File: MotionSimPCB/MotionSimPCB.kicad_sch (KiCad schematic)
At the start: 26 parts, among them J1 Conn_01x02, J10 Conn_01x02, J12 AudioJack2, J2 Conn_01x08_Pin, J3 Conn_01x03, J4 Conn_01x03, J5 Conn_01x03, J6 Conn_01x03, J7 Conn_01x02, J8 Conn_01x02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

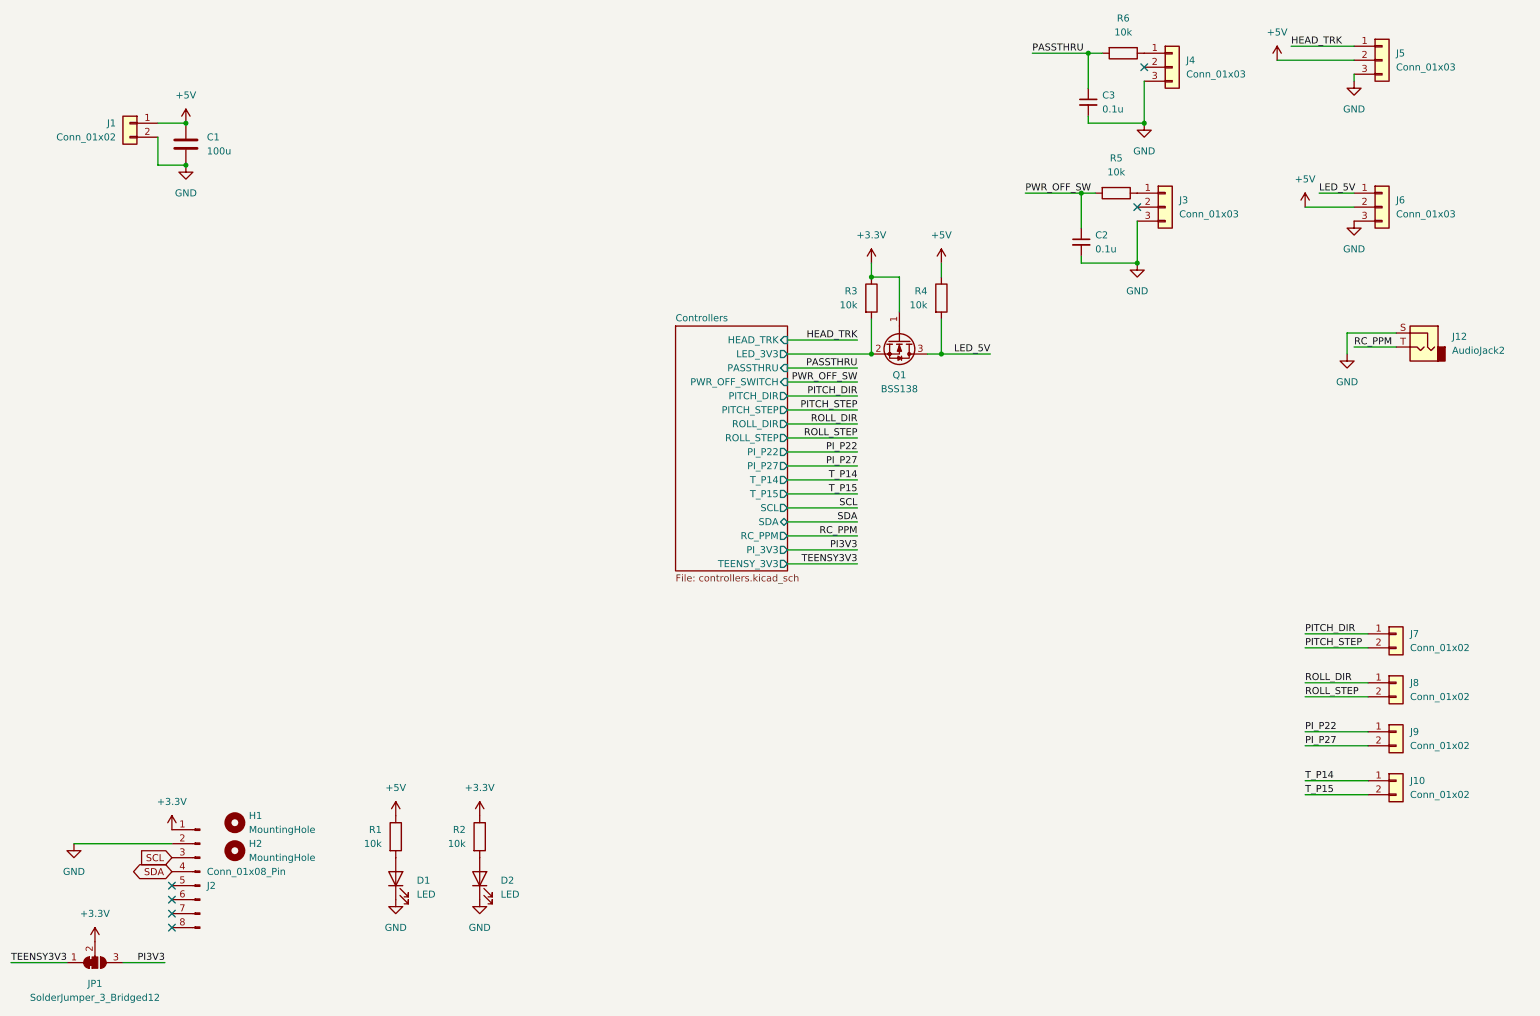
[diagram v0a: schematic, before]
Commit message: fix drc, add protection
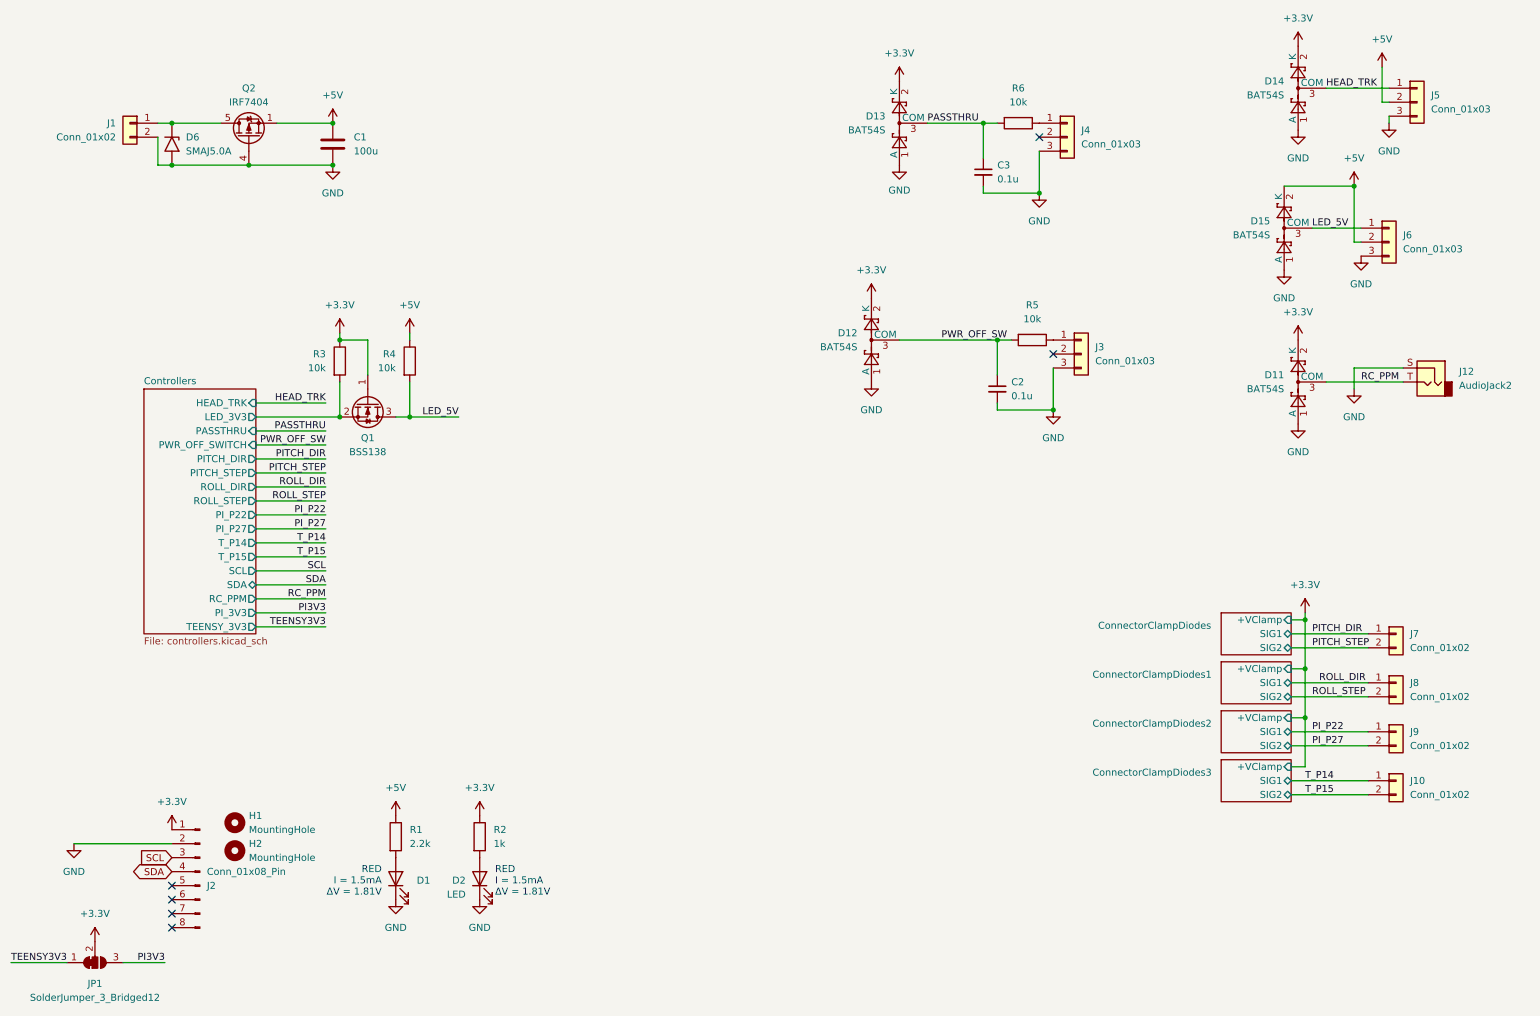
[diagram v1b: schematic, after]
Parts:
- added D11, D12, D13, D14, D15: BAT54S, Package_TO_SOT_SMD:SOT-23, symbol Diode:BAT54S
- added D6: SMAJ5.0A, Diode_SMD:D_SMA, symbol Diode:SMAJ5.0A
- added Q2: IRF7404, Package_SO:SOIC-8_3.9x4.9mm_P1.27mm, symbol Transistor_FET:IRF7404
- D1, D2: JLC PN (none) -> C2286
- R1: value 10k -> 2.2k
- R2: value 10k -> 1k
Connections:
- net +3.3V: now also D11.2 (K), D12.2 (K), D13.2 (K), D14.2 (K)
- net +5V: now also D15.2 (K), Q2.1 (S), Q2.2 (S), Q2.3 (S); no longer J1.1 (Pin_1)
- net GND: now also D11.1 (A), D12.1 (A), D13.1 (A), D14.1 (A), D15.1 (A), D6.2 (A2), Q2.4 (G)
- net HEAD_TRK: now also D14.3 (COM)
- net LED_5V: now also D15.3 (COM)
- net PASSTHRU: now also D13.3 (COM)
- net PWR_OFF_SW: now also D12.3 (COM)
- net RC_PPM: now also D11.3 (COM)
- new net: D6.1 (A1), J1.1 (Pin_1), Q2.5 (D), Q2.6 (D), Q2.7 (D), Q2.8 (D)
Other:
- added sheet ConnectorClampDiodes (connector_clamp_diodes.kicad_sch)
- added sheet ConnectorClampDiodes1 (connector_clamp_diodes.kicad_sch)
- added sheet ConnectorClampDiodes2 (connector_clamp_diodes.kicad_sch)
- added sheet ConnectorClampDiodes3 (connector_clamp_diodes.kicad_sch)
- note added: "RED I = 1.5mA ΔV = 1.81V"
- moved on the sheet: C1, C2, C3, J12, J3, J4, J5, J6, Q1, R3, R4, R5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

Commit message: fix some issues
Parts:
- added C8: 0.1u, Capacitor_SMD:C_0603_1608Metric, symbol Device:C
- added D16: BZV55C12, Diode_SMD:D_MiniMELF, symbol Diode:BZV55C12
- added JP2: SolderJumper_2_Open, Jumper:SolderJumper-2_P1.3mm_Open_TrianglePad1.0x1.5mm, symbol Jumper:SolderJumper_2_Open
- added R13: 100, Capacitor_SMD:C_0603_1608Metric, symbol Device:R
- added R14: 100k, Capacitor_SMD:C_0603_1608Metric, symbol Device:R
- added TP1: TestPoint_Flag, TestPoint:TestPoint_Pad_D2.0mm, symbol Connector:TestPoint_Flag
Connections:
- net +3.3V: now also R5.1, R6.1
- net +5V: now also C8.1, D16.1 (K), JP2.2 (B), R14.1, TP1.1
- net GND: now also R13.2; no longer Q2.4 (G)
- net PASSTHRU: now also J4.1 (Pin_1)
- net PWR_OFF_SW: now also J3.1 (Pin_1)
- net at D6.1 (A1), J1.1 (Pin_1), Q2.5 (D)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: now also JP2.1 (A)
- new net: C8.2, D16.2 (A), Q2.4 (G), R13.1, R14.2
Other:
- moved on the sheet: C1, Q1, Q2, R3, R4, R5, R6

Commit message: fix clearance
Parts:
- added R15, R16, R17, R18, R19, R20, R21, R22, R24, R25: 100, Capacitor_SMD:C_0603_1608Metric, symbol Device:R
- Q2: value IRF7404 -> DMP2040USS
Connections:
- net HEAD_TRK: now also R25.1; no longer D14.3 (COM), J5.1 (Pin_1)
- net PITCH_DIR: now also R15.1; no longer J7.1 (Pin_1)
- net PITCH_STEP: now also R16.1; no longer J7.2 (Pin_2)
- net PI_P22: now also R19.1; no longer J9.1 (Pin_1)
- net PI_P27: now also R20.1; no longer J9.2 (Pin_2)
- net RC_PPM: now also R24.1; no longer D11.3 (COM), J12.T
- net ROLL_DIR: now also R17.1; no longer J8.1 (Pin_1)
- net ROLL_STEP: now also R18.1; no longer J8.2 (Pin_2)
- net T_P14: now also R21.1; no longer J10.1 (Pin_1)
- net T_P15: now also R22.1; no longer J10.2 (Pin_2)
- new net HEAD_TRK_C: D14.3 (COM), J5.1 (Pin_1), R25.2
- new net PITCH_DIR_C: J7.1 (Pin_1), R15.2
- new net PITCH_STEP_C: J7.2 (Pin_2), R16.2
- new net PI_P22_C: J9.1 (Pin_1), R19.2
- new net PI_P27_C: J9.2 (Pin_2), R20.2
- new net RC_PPM_C: D11.3 (COM), J12.T, R24.2
- new net ROLL_DIR_C: J8.1 (Pin_1), R17.2
- new net ROLL_STEP_C: J8.2 (Pin_2), R18.2
- new net T_P14_C: J10.1 (Pin_1), R21.2
- new net T_P15_C: J10.2 (Pin_2), R22.2
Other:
- moved on the sheet: D11, D12, D14, J12

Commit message: DNP D6
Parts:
- D6: now not fitted
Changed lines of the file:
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@@
 		(in_bom yes)
 		(on_board yes)
-		(dnp no)
+		(dnp yes)
 		(property "Reference" "D6"
 			(at 46.99 36.8299 90)
